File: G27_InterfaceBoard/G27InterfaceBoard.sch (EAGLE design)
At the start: 42 parts, among them IC1 LMV321M5, IC2 74AHCT126PW, IC3 74AHCT126PW, J1 Pedal, J2 Shifter, U1 LMV324

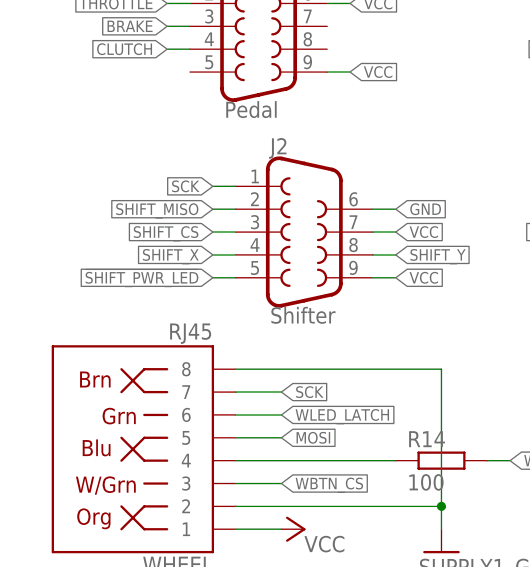
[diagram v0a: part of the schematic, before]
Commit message: Connect shift power LED to ground.
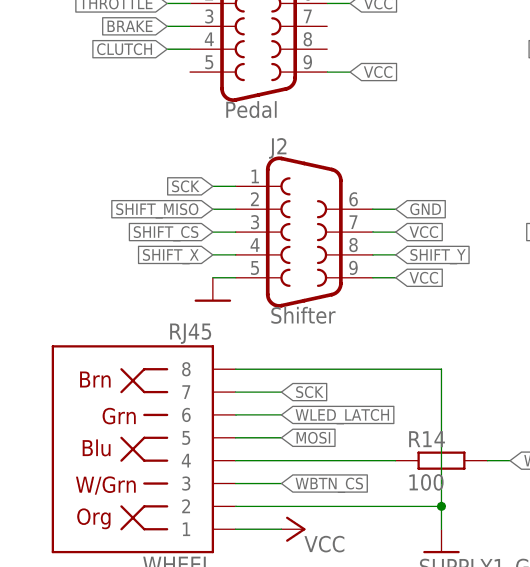
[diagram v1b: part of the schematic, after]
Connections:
- removed net !SHIFT_PWR_LED: J2.5
- net GND: now also J2.5
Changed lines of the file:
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@@
 <part name="D7" library="diode" library_urn="urn:adsk.eagle:library:210" deviceset="BAT54" device="" package3d_urn="urn:adsk.eagle:package:43389/2"/>
 <part name="R11" library="resistor" library_urn="urn:adsk.eagle:library:348" deviceset="R-EU_" device="R0603" package3d_urn="urn:adsk.eagle:package:23555/3" value="5k"/>
+<part name="GND14" library="stm_board_f407" deviceset="SUPPLY1_GND" device=""/>
 </parts>
 <sheets>
@@
 <attribute name="VALUE" x="72.39" y="42.418" size="1.778" layer="96"/>
 </instance>
+<instance part="GND14" gate="1" x="22.86" y="91.44" smashed="yes"/>
 </instances>
 <busses>
@@
 <label x="20.32" y="20.32" size="1.27" layer="95" rot="R180" xref="yes"/>
 </segment>
+<segment>
+<pinref part="J2" gate="G$1" pin="5"/>
+<wire x1="25.4" y1="93.98" x2="22.86" y2="93.98" width="0.1524" layer="91"/>
+<pinref part="GND14" gate="1" pin="GND"/>
+</segment>
 </net>
 <net name="SCK" class="0">
@@
 </segment>
 </net>
-<net name="!SHIFT_PWR_LED" class="0">
-<segment>
-<pinref part="J2" gate="G$1" pin="5"/>
-<wire x1="25.4" y1="93.98" x2="22.86" y2="93.98" width="0.1524" layer="91"/>
-<label x="22.86" y="93.98" size="1.27" layer="95" rot="R180" xref="yes"/>
-</segment>
-</net>
